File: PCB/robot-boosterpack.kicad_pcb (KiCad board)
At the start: 2 copper layers, 60 x 90 mm, 59 parts, among them IC1 DRV8833, IC2 TPS77033, IC3 TPS77050, IC4 LMR61428, J1 3.3V Jumper, J2 5V Jumper, J3 9V Jumper, M1 MOTOR, M2 MOTOR

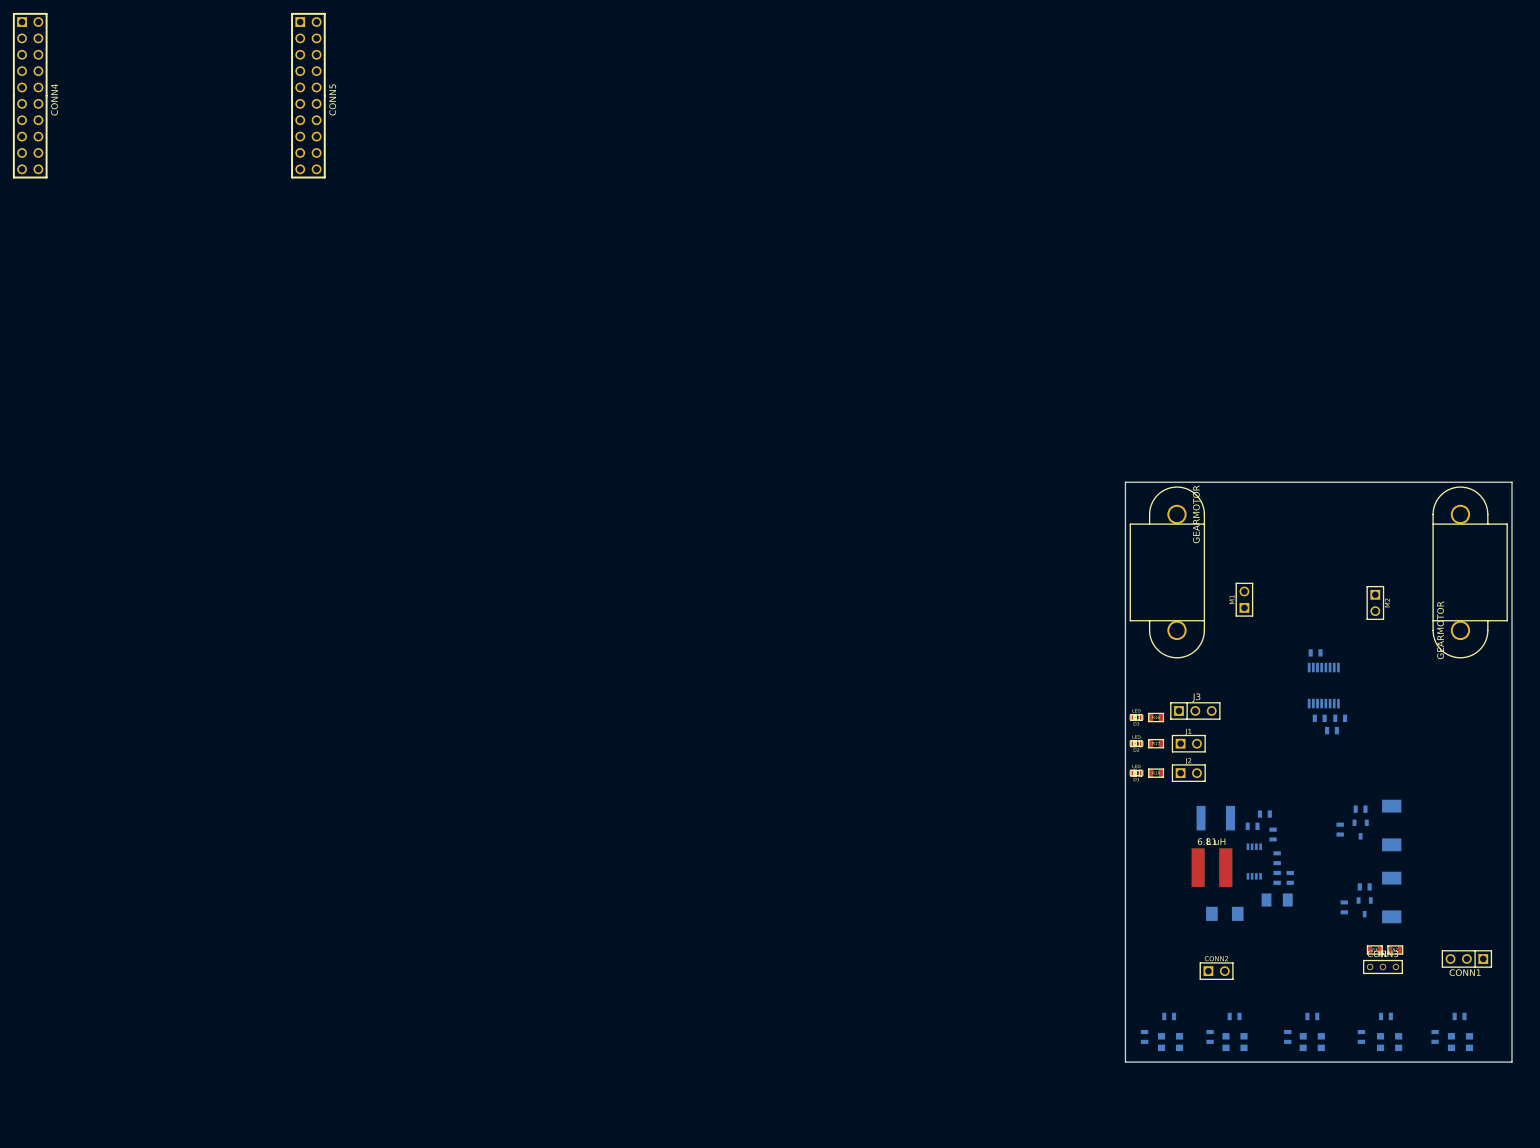
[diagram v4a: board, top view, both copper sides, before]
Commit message: centered LP headers
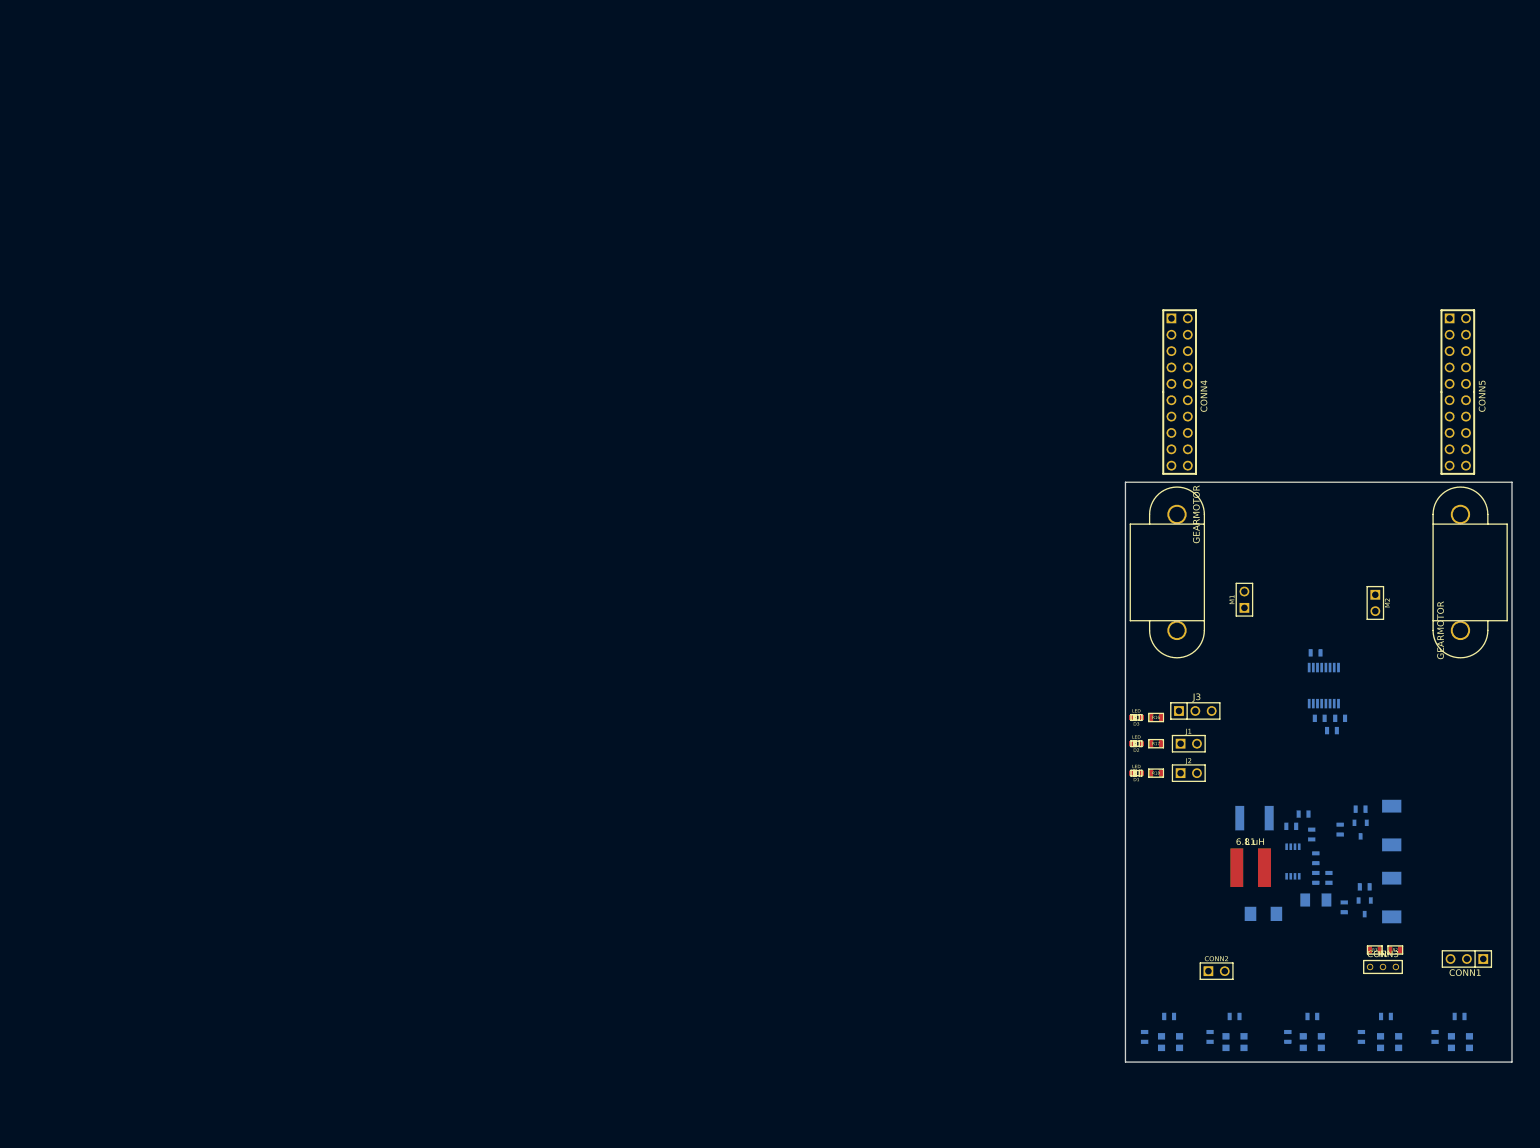
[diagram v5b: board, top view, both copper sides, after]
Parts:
- moved CONN4 184.2 mm to (178.4, 46.0)
- moved CONN5 184.2 mm to (221.6, 46.0)
- moved C10 6.00 mm to (199.5, 121.4)
- moved C11 6.00 mm to (199.5, 124.8)
- moved C8 6.00 mm to (190.0, 112.1)
- moved C9 6.00 mm to (197.6, 111.5)
- moved D4 6.00 mm to (191.4, 127.0)
- moved IC4 6.00 mm to (196.0, 118.9)
- moved L1 6.00 mm to (189.4, 115.8)
- moved R19 6.00 mm to (195.7, 113.4)
- moved R20 6.00 mm to (198.9, 114.7)
- moved R21 6.00 mm to (199.5, 118.4)
- moved R22 6.00 mm to (201.6, 121.4)
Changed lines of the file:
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@@
   )
   (module SM1812 (layer B.Cu)
-    (at 184.023 112.141)
+    (at 190.023 112.141)
     (tags "CMS SM")
     (attr smd)
@@
   )
   (module SM1206POL (layer B.Cu)
-    (at 193.548 124.841)
+    (at 199.548 124.841)
     (attr smd)
     (fp_text reference C11 (at 0 0) (layer B.SilkS)
@@
   )
   (module SM0603_Capa (layer B.Cu)
-    (at 193.548 121.412 270)
+    (at 199.548 121.412 270)
     (attr smd)
     (fp_text reference C10 (at 0 0 540) (layer B.SilkS)
@@
   )
   (module SM0603_Capa (layer B.Cu)
-    (at 191.643 111.506 180)
+    (at 197.643 111.506 180)
     (attr smd)
     (fp_text reference C9 (at 0 0 450) (layer B.SilkS)
@@
   )
   (module SM0603 (layer B.Cu)
-    (at 195.58 121.412 90)
+    (at 201.58 121.412 90)
     (attr smd)
     (fp_text reference R22 (at 0 0 90) (layer B.SilkS)
@@
   )
   (module SM0603 (layer B.Cu)
-    (at 192.913 114.681 270)
+    (at 198.913 114.681 270)
     (attr smd)
     (fp_text reference R20 (at 0 0 270) (layer B.SilkS)
@@
   )
   (module SM0603 (layer B.Cu)
-    (at 193.548 118.364 90)
+    (at 199.548 118.364 90)
     (attr smd)
     (fp_text reference R21 (at 0 0 90) (layer B.SilkS)
@@
   )
   (module SM0603 (layer B.Cu)
-    (at 189.738 113.411)
+    (at 195.738 113.411)
     (attr smd)
     (fp_text reference R19 (at 0 0) (layer B.SilkS)
@@
   )
   (module PIN_ARRAY_10x2 (layer F.Cu)
-    (at 43.18 0 270)
+    (at 221.59 46 270)
     (descr "Double rangee de contacts 2 x 5 pins")
     (tags CONN)
@@
   )
   (module PIN_ARRAY_10x2 (layer F.Cu)
-    (at 0 0 270)
+    (at 178.41 46 270)
     (descr "Double rangee de contacts 2 x 5 pins")
     (tags CONN)
@@
   )
   (module MSOP-8 (layer B.Cu)
-    (at 189.992 118.872)
+    (at 195.992 118.872)
     (descr MSOIC-8)
     (attr smd)
@@
   )
   (module INDUCTOR_SRN6045 (layer F.Cu)
-    (at 183.388 115.824)
+    (at 189.388 115.824)
     (fp_text reference L1 (at 0 0) (layer F.SilkS)
       (effects (font (size 1 1) (thickness 0.15)))
@@
   )
   (module "DO-214AA(SMB)" (layer B.Cu)
-    (at 185.42 127)
+    (at 191.42 127)
     (descr "DO-214AA (SMB)  PACKAGE.")
     (tags "DO-214AA SMB")

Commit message: fixed motor mount orientation
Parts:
- moved GEARMOTOR 18.2 mm to (175.0, 83.0), turned to 90 degrees
- moved GEARMOTOR 18.2 mm to (225.0, 65.0), turned to 270 degrees
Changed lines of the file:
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@@
   )
   (module 1pin (layer F.Cu)
-    (at 178 65 270)
+    (at 175 83 90)
+    (descr "module 1 pin (ou trou mecanique de percage)")
+    (tags DEV)
+    (path 1pin)
+    (fp_text reference GEARMOTOR (at 0 -3.048 90) (layer F.SilkS)
+      (effects (font (size 1.016 1.016) (thickness 0.254)))
+    )
+    (fp_text value P*** (at 0 2.794 90) (layer F.SilkS) hide
+      (effects (font (size 1.016 1.016) (thickness 0.254)))
+    )
+    (fp_line (start 16.5 4.25) (end 18 4.25) (layer F.SilkS) (width 0.15))
+    (fp_line (start 0 4.25) (end 1.5 4.25) (layer F.SilkS) (width 0.15))
+    (fp_line (start 1.5 7.25) (end 1.5 -4.25) (layer F.SilkS) (width 0.15))
+    (fp_line (start 16.5 -4.25) (end 16.5 7.25) (layer F.SilkS) (width 0.15))
+    (fp_line (start 1.5 7.25) (end 16.5 7.25) (layer F.SilkS) (width 0.15))
+    (fp_line (start 0 -4.25) (end 18 -4.25) (layer F.SilkS) (width 0.15))
+    (fp_arc (start 18 0) (end 18 -4.25) (angle 180) (layer F.SilkS) (width 0.15))
+    (fp_arc (start 0 0) (end 0 4.25) (angle 180) (layer F.SilkS) (width 0.15))
+    (pad 1 thru_hole circle (at 0 0 90) (size 3 3) (drill 2.39)
+      (layers *.Cu *.Mask F.SilkS)
+    )
+    (pad 2 thru_hole circle (at 18 0 90) (size 3 3) (drill 2.39)
+      (layers *.Cu *.Mask F.SilkS)
+    )
+  )
+  (module 1pin (layer F.Cu)
+    (at 225 65 270)
     (descr "module 1 pin (ou trou mecanique de percage)")
     (tags DEV)
@@
       (layers *.Cu *.Mask F.SilkS)
     )
-  )
-  (module 1pin (layer F.Cu)
-    (at 222 83 90)
-    (descr "module 1 pin (ou trou mecanique de percage)")
-    (tags DEV)
-    (path 1pin)
-    (fp_text reference GEARMOTOR (at 0 -3.048 90) (layer F.SilkS)
-      (effects (font (size 1.016 1.016) (thickness 0.254)))
-    )
-    (fp_text value P*** (at 0 2.794 90) (layer F.SilkS) hide
-      (effects (font (size 1.016 1.016) (thickness 0.254)))
-    )
-    (fp_line (start 16.5 4.25) (end 18 4.25) (layer F.SilkS) (width 0.15))
-    (fp_line (start 0 4.25) (end 1.5 4.25) (layer F.SilkS) (width 0.15))
-    (fp_line (start 1.5 7.25) (end 1.5 -4.25) (layer F.SilkS) (width 0.15))
-    (fp_line (start 16.5 -4.25) (end 16.5 7.25) (layer F.SilkS) (width 0.15))
-    (fp_line (start 1.5 7.25) (end 16.5 7.25) (layer F.SilkS) (width 0.15))
-    (fp_line (start 0 -4.25) (end 18 -4.25) (layer F.SilkS) (width 0.15))
-    (fp_arc (start 18 0) (end 18 -4.25) (angle 180) (layer F.SilkS) (width 0.15))
-    (fp_arc (start 0 0) (end 0 4.25) (angle 180) (layer F.SilkS) (width 0.15))
-    (pad 1 thru_hole circle (at 0 0 90) (size 3 3) (drill 2.39)
-      (layers *.Cu *.Mask F.SilkS)
-    )
-    (pad 2 thru_hole circle (at 18 0 90) (size 3 3) (drill 2.39)
-      (layers *.Cu *.Mask F.SilkS)
-    )

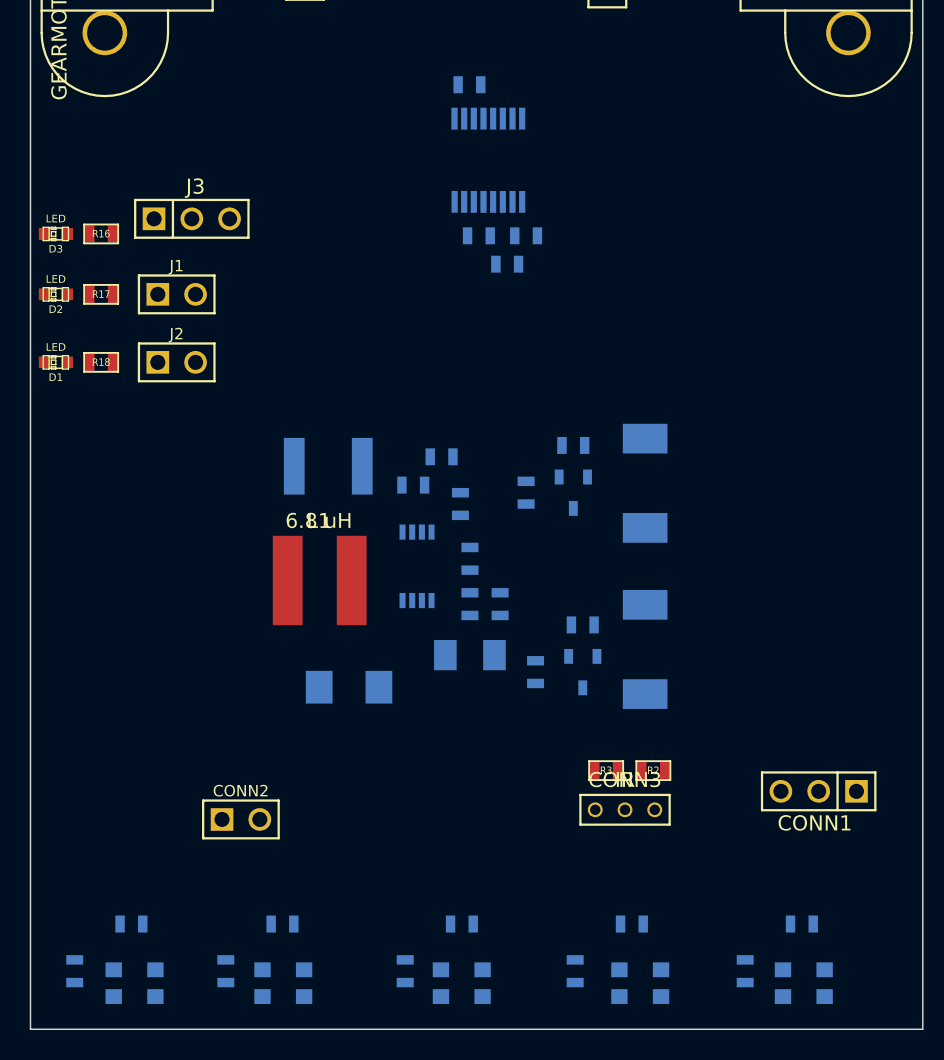
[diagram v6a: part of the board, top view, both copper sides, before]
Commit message: modified reflectance sensor module and placement
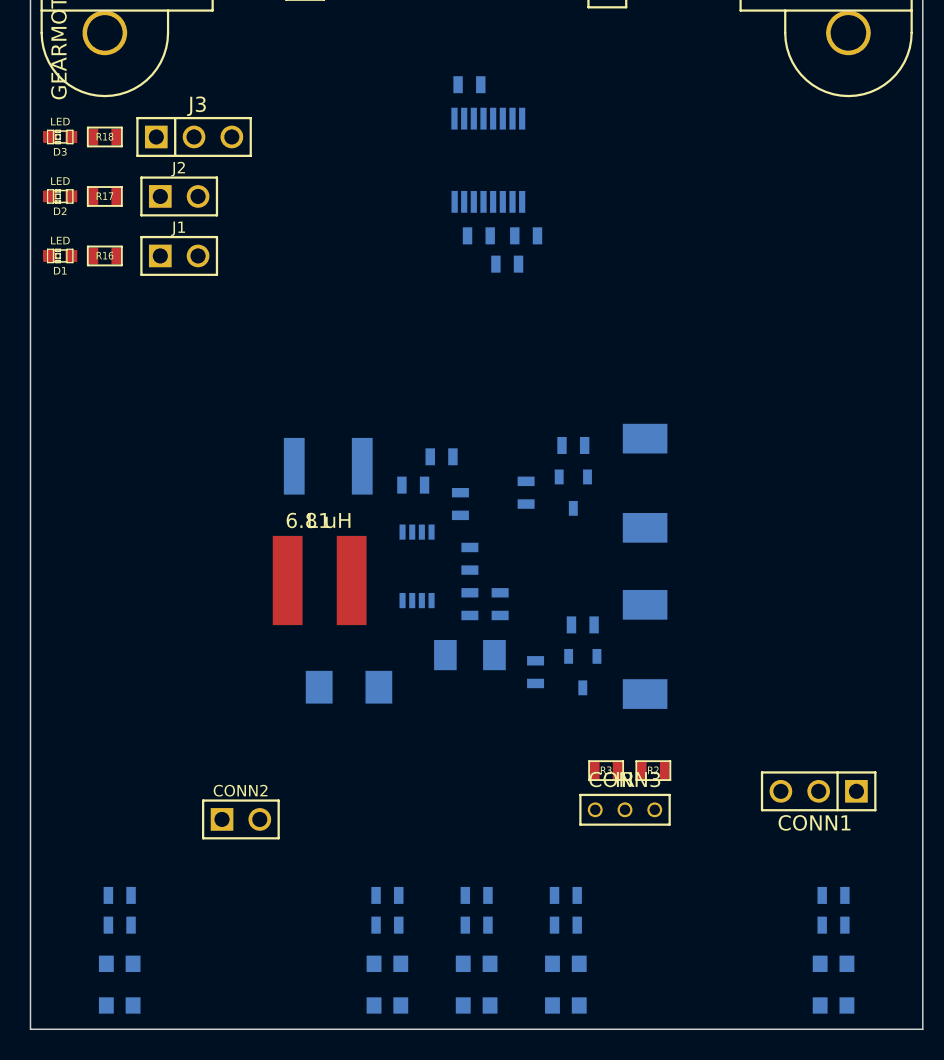
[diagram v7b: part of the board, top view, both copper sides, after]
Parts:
- moved R18 15.2 mm to (175.0, 90.0)
- moved R6 12.0 mm to (194.0, 141.0), turned to 0 degrees
- moved J2 11.2 mm to (180.0, 94.0)
- moved R14 7.83 mm to (224.0, 141.0), turned to 0 degrees
- moved IR2 7.62 mm to (194.0, 147.0), turned to 90 degrees
- moved D1 7.16 mm to (172.0, 98.0)
- moved R7 7.06 mm to (194.0, 143.0)
- moved D2 6.59 mm to (172.0, 94.0)
- moved R17 6.59 mm to (175.0, 94.0)
- moved D3 6.53 mm to (172.0, 90.0)
- moved R1 5.93 mm to (176.0, 141.0), turned to 0 degrees
- moved IR4 5.83 mm to (206.0, 147.0), turned to 90 degrees
- moved R8 5.71 mm to (200.0, 143.0), turned to 0 degrees
- moved J3 5.51 mm to (181.0, 90.0)
- moved R12 5.14 mm to (206.0, 141.0), turned to 0 degrees
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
